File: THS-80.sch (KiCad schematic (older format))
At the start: 27 parts, among them J1 USB_B_Micro, J2 IDE, J3 RC80 Bus, J4 RC80 Bus, U1 MAX40200AUK

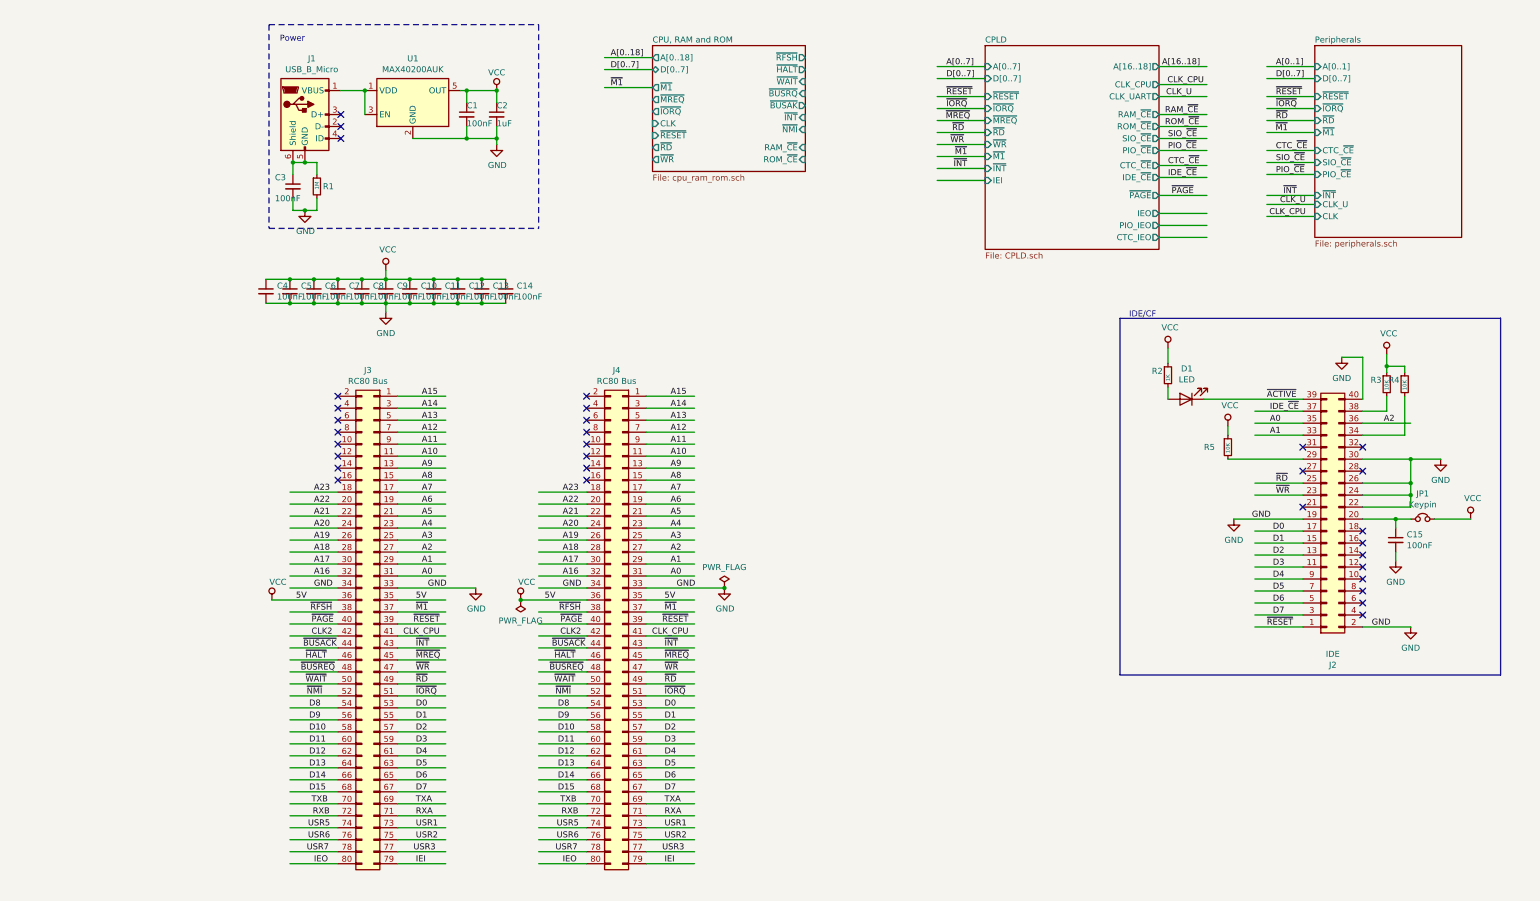
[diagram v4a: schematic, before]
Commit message: fixed bus connections
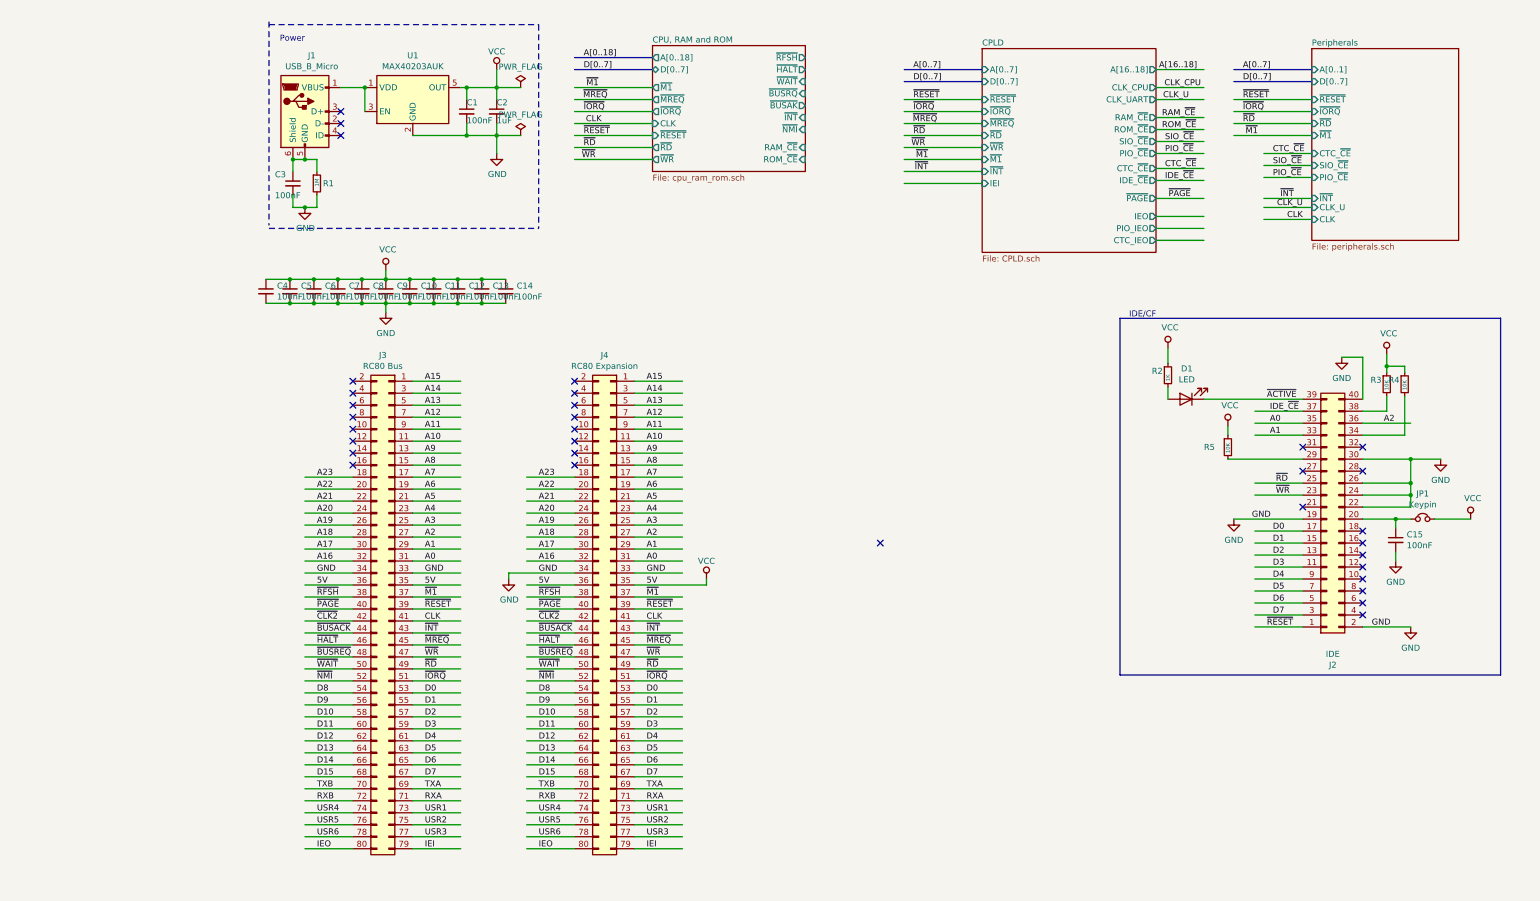
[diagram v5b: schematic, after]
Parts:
- J1: footprint Connector_USB:USB_Micro-B_Molex-105017-0001 -> Connector_USB:USB_Micro-B_Amphenol_10103594-0001LF_Horizontal
- J4: value RC80 Bus -> RC80 Expansion
- U1: value MAX40200AUK -> MAX40203AUK; MPN MAX40200AUK+T -> MAX40203AUK+T; Mouser PN 700-MAX40200AUK+T -> 700-MAX40203AUK+T
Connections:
- net labels added: CLK, USR4, ~CLK2
- net labels removed: A[0..1], CLK2, USR7
- wire segments 268 -> 273
- no-connect marks 32 -> 33
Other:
- moved on the sheet: C1, C2, C3, J1, R1, U1

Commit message: passed DRC
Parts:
- removed C10, C11, C12, C13, C14, C4, C5, C6, C7, C8, C9: 100nF, Capacitor_SMD:C_0603_1608Metric_Pad1.05x0.95mm_HandSolder, symbol Device:C_Small
- added R2, R3, R4, R5: 10K, Resistor_SMD:R_0603_1608Metric_Pad1.05x0.95mm_HandSolder, symbol Device:R_Small
- added SW1: Reset, Button_Switch_SMD:SW_SPST_FSMSM, symbol Switch:SW_Push
- added U2: DS1813R-5+T&R, Package_TO_SOT_SMD:SOT-23, symbol THS-80:DS1813R-5+T&R
- renumbered C3 to C1, C1 to C2, C2 to C3, C15 to C4, J3 to J2, J4 to J3, J2 to J4, R2 to R6, R5 to R7, R3 to R8, R4 to R9
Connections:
- net labels added: A[0..1], RAM_~CE, ROM_~CE, ~BUSAK, ~BUSRQ
- net labels removed: RAM_~CE~, ROM_~CE~, ~BUSACK, ~BUSREQ
- no-connect marks 33 -> 32

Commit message: started routing
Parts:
- added C22: 100uF, Capacitor_SMD:C_1206_3216Metric_Pad1.42x1.75mm_HandSolder, symbol Device:C_Small
- added C23: 100nF, Capacitor_SMD:C_0603_1608Metric_Pad1.05x0.95mm_HandSolder, symbol Device:C_Small
- C2: value 100nF -> 2.2nF
- C3: value 1uF -> .33uF
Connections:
- wire segments 273 -> 274
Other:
- moved on the sheet: C2, C3, C4, D1, J4, JP1, R6, R7, R8, R9, SW1, U2

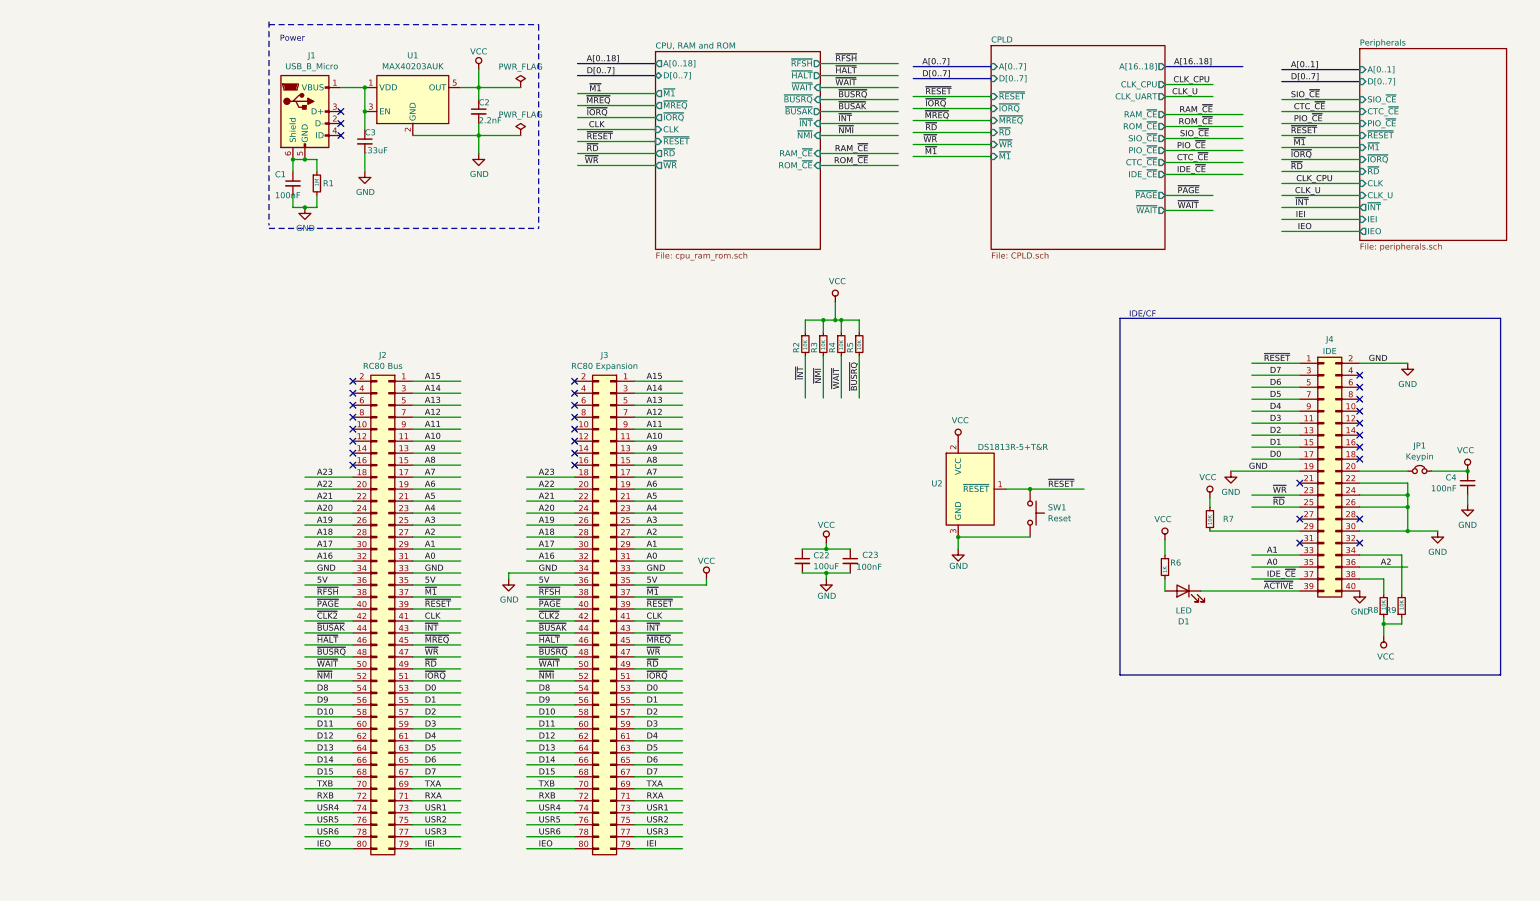
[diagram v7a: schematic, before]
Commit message: finished routing, passed DRC
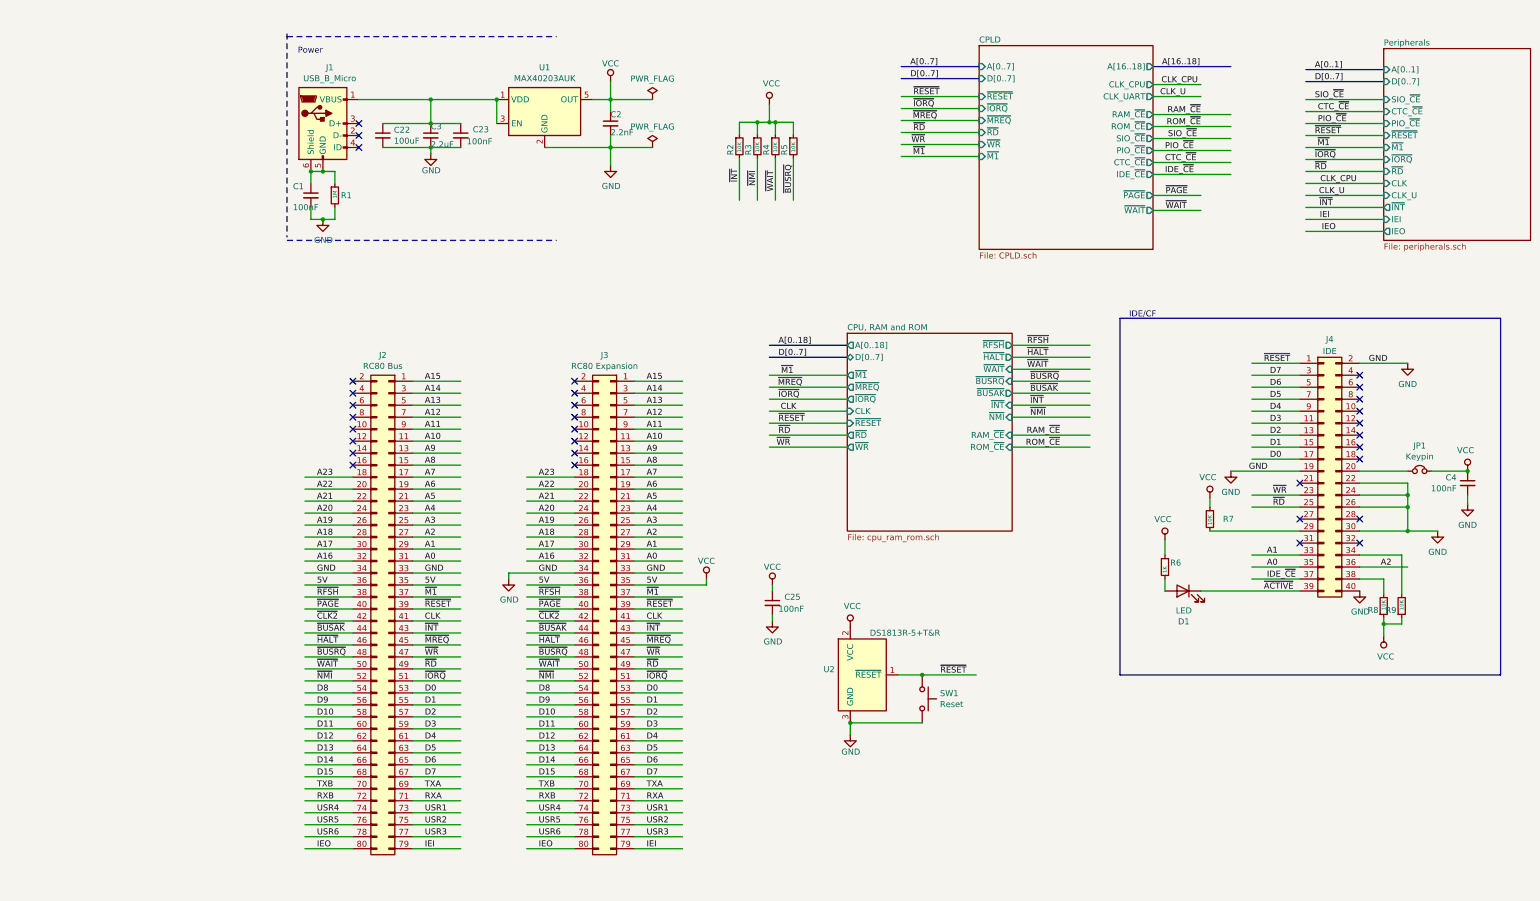
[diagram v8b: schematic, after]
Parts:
- added C25: 100nF, Capacitor_SMD:C_0603_1608Metric_Pad1.05x0.95mm_HandSolder, symbol Device:C_Small
- C3: value .33uF -> 2.2uF
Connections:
- wire segments 274 -> 275
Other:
- moved on the sheet: C1, C2, C22, C23, C3, J1, R1, R2, R3, R4, R5, SW1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
